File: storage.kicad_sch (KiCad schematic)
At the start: 18 parts, among them J5 Micro_SD_Card_Det1, U1 MIMX8MM6DVTLZAA, U15 W25Q32JWZP, U30 TPD4EUSB30, U31 D5V0H1B2LP, U32 SiP32431DR3, U33 TPD4EUSB30

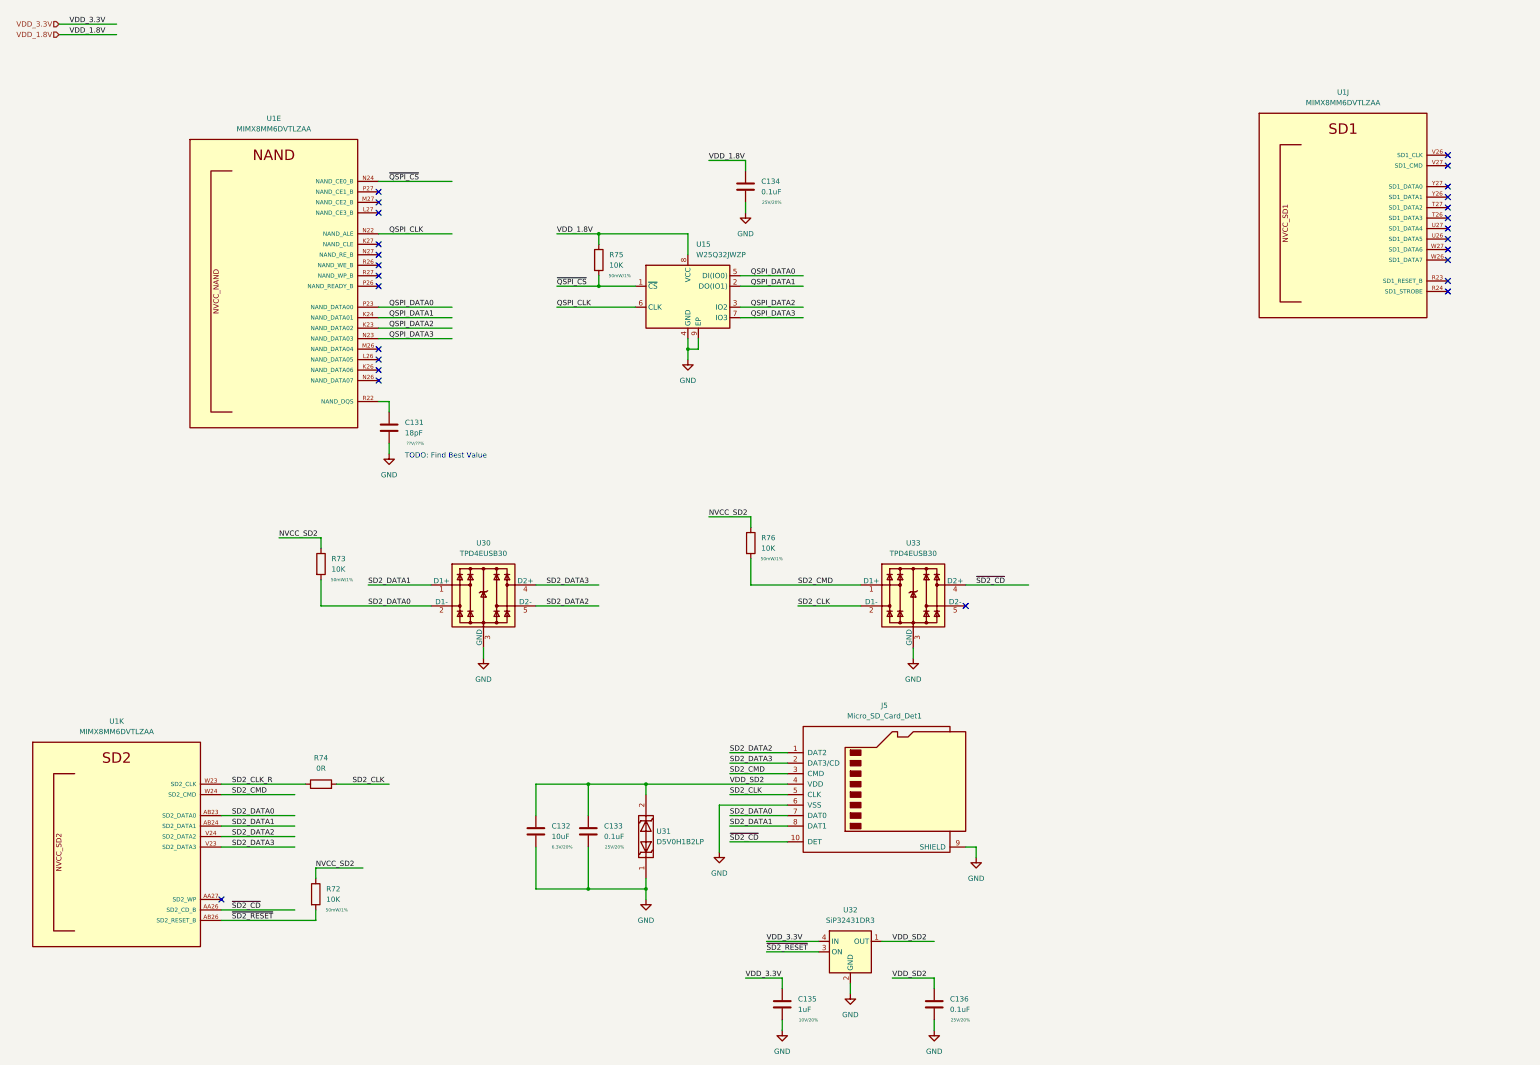
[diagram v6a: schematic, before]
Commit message: fix ref desgigators, add table for dram config
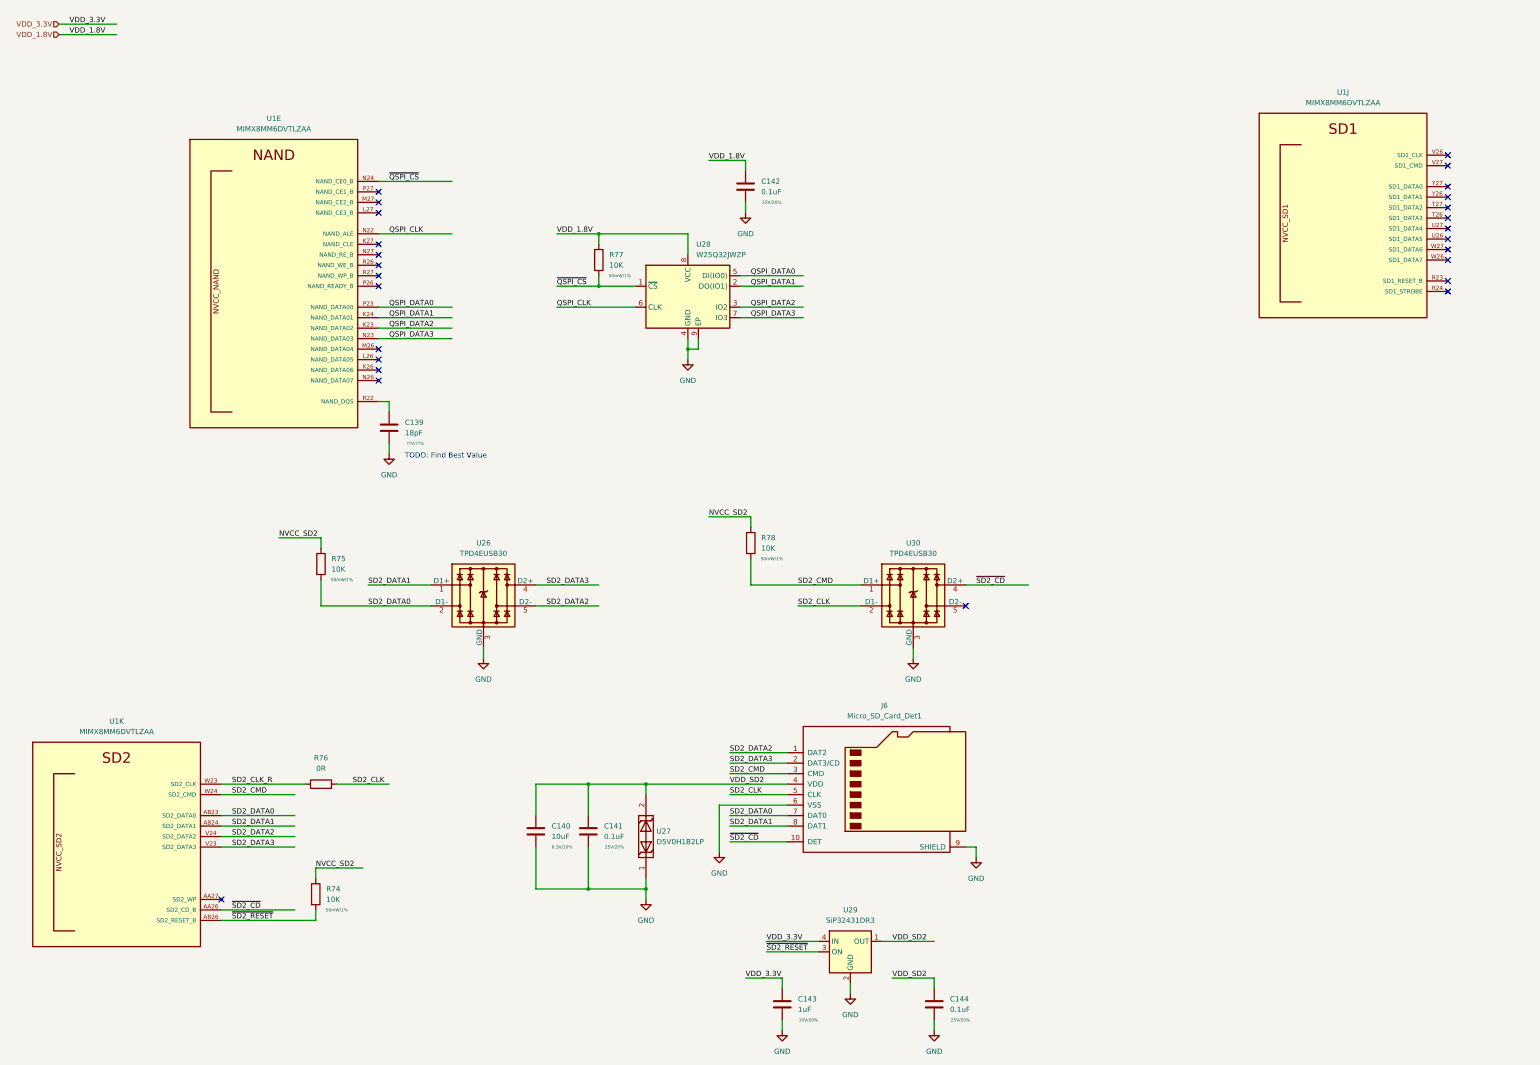
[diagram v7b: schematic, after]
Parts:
- renumbered C131 to C139, C132 to C140, C133 to C141, C134 to C142, C135 to C143, C136 to C144, J5 to J6, R72 to R74, R73 to R75, R74 to R76, R75 to R77, R76 to R78, U30 to U26, U31 to U27, U15 to U28, U32 to U29, U33 to U30
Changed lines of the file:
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@@
   (symbol (lib_id "Device:C") (at 144.78 214.63 0) (unit 1)
     (in_bom yes) (on_board yes)
-    (property "Reference" "C132" (id 0) (at 148.59 213.3599 0)
+    (property "Reference" "C140" (id 0) (at 148.59 213.3599 0)
       (effects (font (size 1.27 1.27)) (justify left))
     )
@@
   (symbol (lib_id "Device:R") (at 92.71 203.2 90) (unit 1)
     (in_bom yes) (on_board yes) (fields_autoplaced)
-    (property "Reference" "R74" (id 0) (at 92.71 196.85 90))
+    (property "Reference" "R76" (id 0) (at 92.71 196.85 90))
     (property "Value" "0R" (id 1) (at 92.71 199.39 90))
     (property "Footprint" "Resistor_SMD:R_0402_1005Metric" (id 2) (at 92.71 204.978 90)
@@
   (symbol (lib_id "qsbc:Micro_SD_Card_Det1") (at 228.6 203.2 0) (unit 1)
     (in_bom yes) (on_board yes) (fields_autoplaced)
-    (property "Reference" "J5" (id 0) (at 229.235 184.15 0))
+    (property "Reference" "J6" (id 0) (at 229.235 184.15 0))
     (property "Value" "Micro_SD_Card_Det1" (id 1) (at 229.235 186.69 0))
     (property "Footprint" "qsbc:GCT_MEM2051-00-195-00-A_REVC" (id 2) (at 257.81 195.58 0)
@@
   (symbol (lib_id "power:GND") (at 195.58 64.77 0) (unit 1)
     (in_bom yes) (on_board yes) (fields_autoplaced)
-    (property "Reference" "#PWR0217" (id 0) (at 195.58 71.12 0)
+    (property "Reference" "#PWR0127" (id 0) (at 195.58 71.12 0)
       (effects (font (size 1.27 1.27)) hide)
     )
@@
   (symbol (lib_id "power:GND") (at 236.22 172.72 0) (unit 1)
     (in_bom yes) (on_board yes) (fields_autoplaced)
-    (property "Reference" "#PWR0222" (id 0) (at 236.22 179.07 0)
+    (property "Reference" "#PWR0130" (id 0) (at 236.22 179.07 0)
       (effects (font (size 1.27 1.27)) hide)
     )
@@
   (symbol (lib_id "Device:R") (at 92.71 149.86 0) (unit 1)
     (in_bom yes) (on_board yes)
-    (property "Reference" "R73" (id 0) (at 95.25 148.5899 0)
+    (property "Reference" "R75" (id 0) (at 95.25 148.5899 0)
       (effects (font (size 1.27 1.27)) (justify left))
     )
@@
   (symbol (lib_id "power:GND") (at 241.3 262.89 0) (unit 1)
     (in_bom yes) (on_board yes) (fields_autoplaced)
-    (property "Reference" "#PWR0216" (id 0) (at 241.3 269.24 0)
+    (property "Reference" "#PWR0131" (id 0) (at 241.3 269.24 0)
       (effects (font (size 1.27 1.27)) hide)
     )
@@
   (symbol (lib_id "power:GND") (at 251.46 220.98 0) (unit 1)
     (in_bom yes) (on_board yes) (fields_autoplaced)
-    (property "Reference" "#PWR0215" (id 0) (at 251.46 227.33 0)
+    (property "Reference" "#PWR0132" (id 0) (at 251.46 227.33 0)
       (effects (font (size 1.27 1.27)) hide)
     )
@@
   (symbol (lib_id "power:GND") (at 109.22 123.19 0) (unit 1)
     (in_bom yes) (on_board yes) (fields_autoplaced)
-    (property "Reference" "#PWR0219" (id 0) (at 109.22 129.54 0)
+    (property "Reference" "#PWR0122" (id 0) (at 109.22 129.54 0)
       (effects (font (size 1.27 1.27)) hide)
     )
@@
   (symbol (lib_id "Device:C") (at 204.47 256.54 0) (unit 1)
     (in_bom yes) (on_board yes)
-    (property "Reference" "C135" (id 0) (at 208.28 255.2699 0)
+    (property "Reference" "C143" (id 0) (at 208.28 255.2699 0)
       (effects (font (size 1.27 1.27)) (justify left))
     )
@@
   (symbol (lib_id "power:GND") (at 171.45 231.14 0) (unit 1)
     (in_bom yes) (on_board yes) (fields_autoplaced)
-    (property "Reference" "#PWR0221" (id 0) (at 171.45 237.49 0)
+    (property "Reference" "#PWR0124" (id 0) (at 171.45 237.49 0)
       (effects (font (size 1.27 1.27)) hide)
     )
@@
   (symbol (lib_id "power:GND") (at 189.23 219.71 0) (unit 1)
     (in_bom yes) (on_board yes) (fields_autoplaced)
-    (property "Reference" "#PWR0220" (id 0) (at 189.23 226.06 0)
+    (property "Reference" "#PWR0126" (id 0) (at 189.23 226.06 0)
       (effects (font (size 1.27 1.27)) hide)
     )
@@
   (symbol (lib_id "qsbc:TPD4EUSB30") (at 236.22 157.48 0) (unit 1)
     (in_bom yes) (on_board yes) (fields_autoplaced)
-    (property "Reference" "U33" (id 0) (at 236.22 144.78 0))
+    (property "Reference" "U30" (id 0) (at 236.22 144.78 0))
     (property "Value" "TPD4EUSB30" (id 1) (at 236.22 147.32 0))
     (property "Footprint" "Package_SON:USON-10_2.5x1.0mm_P0.5mm" (id 2) (at 212.09 167.64 0)
@@
   (symbol (lib_id "Memory_Flash:W25Q32JVZP") (at 181.61 85.09 0) (unit 1)
     (in_bom yes) (on_board yes) (fields_autoplaced)
-    (property "Reference" "U15" (id 0) (at 183.6294 72.39 0)
+    (property "Reference" "U28" (id 0) (at 183.6294 72.39 0)
       (effects (font (size 1.27 1.27)) (justify left))
     )
@@
   (symbol (lib_id "qsbc:D5V0H1B2LP") (at 170.18 215.9 90) (unit 1)
     (in_bom yes) (on_board yes) (fields_autoplaced)
-    (property "Reference" "U31" (id 0) (at 173.99 214.6299 90)
+    (property "Reference" "U27" (id 0) (at 173.99 214.6299 90)
       (effects (font (size 1.27 1.27)) (justify right))
     )
@@
   (symbol (lib_id "Device:R") (at 196.85 144.78 0) (unit 1)
     (in_bom yes) (on_board yes)
-    (property "Reference" "R76" (id 0) (at 199.39 143.5099 0)
+    (property "Reference" "R78" (id 0) (at 199.39 143.5099 0)
       (effects (font (size 1.27 1.27)) (justify left))
     )
@@
   (symbol (lib_id "Power_Management:SiP32431DR3") (at 220.98 243.84 0) (unit 1)
     (in_bom yes) (on_board yes) (fields_autoplaced)
-    (property "Reference" "U32" (id 0) (at 220.98 233.68 0))
+    (property "Reference" "U29" (id 0) (at 220.98 233.68 0))
     (property "Value" "SiP32431DR3" (id 1) (at 220.98 236.22 0))
     (property "Footprint" "Package_TO_SOT_SMD:SOT-363_SC-70-6" (id 2) (at 220.98 232.41 0)
@@
   (symbol (lib_id "power:GND") (at 204.47 262.89 0) (unit 1)
     (in_bom yes) (on_board yes) (fields_autoplaced)
-    (property "Reference" "#PWR0214" (id 0) (at 204.47 269.24 0)
+    (property "Reference" "#PWR0128" (id 0) (at 204.47 269.24 0)
       (effects (font (size 1.27 1.27)) hide)
     )
@@
   (symbol (lib_id "qsbc:TPD4EUSB30") (at 132.08 157.48 0) (unit 1)
     (in_bom yes) (on_board yes) (fields_autoplaced)
-    (property "Reference" "U30" (id 0) (at 132.08 144.78 0))
+    (property "Reference" "U26" (id 0) (at 132.08 144.78 0))
     (property "Value" "TPD4EUSB30" (id 1) (at 132.08 147.32 0))
     (property "Footprint" "Package_SON:USON-10_2.5x1.0mm_P0.5mm" (id 2) (at 107.95 167.64 0)
@@
   (symbol (lib_id "Device:C") (at 157.48 214.63 0) (unit 1)
     (in_bom yes) (on_board yes)
-    (property "Reference" "C133" (id 0) (at 161.29 213.3599 0)
+    (property "Reference" "C141" (id 0) (at 161.29 213.3599 0)
       (effects (font (size 1.27 1.27)) (justify left))
     )
@@
   (symbol (lib_id "Device:C") (at 195.58 58.42 0) (unit 1)
     (in_bom yes) (on_board yes)
-    (property "Reference" "C134" (id 0) (at 199.39 57.1499 0)
+    (property "Reference" "C142" (id 0) (at 199.39 57.1499 0)
       (effects (font (size 1.27 1.27)) (justify left))
     )
@@
   (symbol (lib_id "Device:R") (at 91.44 229.87 0) (unit 1)
     (in_bom yes) (on_board yes)
-    (property "Reference" "R72" (id 0) (at 93.98 228.5999 0)
+    (property "Reference" "R74" (id 0) (at 93.98 228.5999 0)
       (effects (font (size 1.27 1.27)) (justify left))
     )
@@
   (symbol (lib_id "Device:R") (at 160.02 76.2 0) (unit 1)
     (in_bom yes) (on_board yes)
-    (property "Reference" "R75" (id 0) (at 162.56 74.9299 0)
+    (property "Reference" "R77" (id 0) (at 162.56 74.9299 0)
       (effects (font (size 1.27 1.27)) (justify left))
     )
@@
   (symbol (lib_id "power:GND") (at 132.08 172.72 0) (unit 1)
     (in_bom yes) (on_board yes) (fields_autoplaced)
-    (property "Reference" "#PWR0223" (id 0) (at 132.08 179.07 0)
+    (property "Reference" "#PWR0123" (id 0) (at 132.08 179.07 0)
       (effects (font (size 1.27 1.27)) hide)
     )
@@
   (symbol (lib_id "power:GND") (at 181.61 100.33 0) (unit 1)
     (in_bom yes) (on_board yes) (fields_autoplaced)
-    (property "Reference" "#PWR0218" (id 0) (at 181.61 106.68 0)
+    (property "Reference" "#PWR0125" (id 0) (at 181.61 106.68 0)
       (effects (font (size 1.27 1.27)) hide)
     )
@@
   (symbol (lib_id "Device:C") (at 109.22 116.84 0) (unit 1)
     (in_bom yes) (on_board yes)
-    (property "Reference" "C131" (id 0) (at 113.03 115.5699 0)
+    (property "Reference" "C139" (id 0) (at 113.03 115.5699 0)
       (effects (font (size 1.27 1.27)) (justify left))
     )
@@
   (symbol (lib_id "power:GND") (at 220.98 254 0) (unit 1)
     (in_bom yes) (on_board yes) (fields_autoplaced)
-    (property "Reference" "#PWR0213" (id 0) (at 220.98 260.35 0)
+    (property "Reference" "#PWR0129" (id 0) (at 220.98 260.35 0)
       (effects (font (size 1.27 1.27)) hide)
     )
@@
   (symbol (lib_id "Device:C") (at 241.3 256.54 0) (unit 1)
     (in_bom yes) (on_board yes)
-    (property "Reference" "C136" (id 0) (at 245.11 255.2699 0)
-      (effects (font (size 1.27 1.27)) (justify left))
-    )
+    (property "Reference" "C144" (id 0) (at 245.11 255.2699 0)
+      (effects (font (size 1.27 1.27)) (justify left))
+    )
